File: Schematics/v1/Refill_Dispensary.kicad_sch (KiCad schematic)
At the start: 67 parts, among them J1 USB_B_Micro, J10 Switch 2, J11 Switch 3, J12 Switch 1, J13 SWD, J14 SWD, J15 Screen data, J16 Screen Backlight, J2 Pot 1, J3 Barrel_Jack_Switch, J4 USB_BOOT, J5 Load Cell Power, J6 Load Cell Data, J7 Inductor 1, J8 Inductor 2, J9 Pot 2, Q1 TIP120, Q2 TIP120, SW4 SW_SPDT, U1 RP2040, U2 NCP1117-3.3_SOT223, U3 Flash Memory, U5 AD622, Y1 Crystal

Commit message: cleanup
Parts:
- removed J15: Screen data, Connector_JST:JST_XH_B4B-XH-AM_1x04_P2.50mm_Vertical, symbol Connector_Generic:Conn_01x04
- removed J16: Screen Backlight, Connector_JST:JST_XH_B4B-XH-AM_1x04_P2.50mm_Vertical, symbol Connector_Generic:Conn_01x04
- added U4: NHD-C0220BIZ, Display:NHD-C0220BiZ, symbol Display_Character:NHD-C0220BIZ
- C1, C10, C13, C15, C16, C4, C7, C9: footprint Capacitor_SMD:C_0603_1608Metric_Pad1.08x0.95mm_HandSolder -> Capacitor_SMD:C_0402_1005Metric
- C11: value 1u -> 100n; footprint Capacitor_SMD:C_0603_1608Metric_Pad1.08x0.95mm_HandSolder -> Capacitor_SMD:C_0402_1005Metric
- C12: value 100n -> 1u; footprint Capacitor_SMD:C_0603_1608Metric_Pad1.08x0.95mm_HandSolder -> Capacitor_SMD:C_0201_0603Metric
- C14, C8: footprint Capacitor_SMD:C_0603_1608Metric_Pad1.08x0.95mm_HandSolder -> Capacitor_SMD:C_0201_0603Metric
- R1, R10, R11, R13, R14, R16, R2, R3, R4, R5, R6, R7, R8: footprint Resistor_SMD:R_0603_1608Metric_Pad0.98x0.95mm_HandSolder -> Resistor_SMD:R_0201_0603Metric
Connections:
- net +1V1: now also C1.2, C7.2; no longer C1.1, C7.1
- net +3.3V: now also C10.2, C11.2, C13.2, C15.2, C16.2, C9.2, R13.1, U4.5 (VDD), U4.9 (A); no longer C10.1, C11.1, C13.1, C15.1, C16.1, C9.1, R13.2
- net GND: now also C1.1, C10.1, C11.1, C13.1, C15.1, C16.1, C7.1, C9.1, U4.10 (K), U4.4 (VSS); no longer C1.2, C10.2, C11.2, C13.2, C15.2, C16.2, C7.2, C9.2
- net S_SCL: now also R13.2, U4.2 (SCL); no longer R13.1
- net S_SDA: now also U4.3 (SDA)
- net at C14.2: now also U4.8 (C1-)
- net at C14.1: now also U4.7 (C1+)
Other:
- moved on the sheet: C14, R10

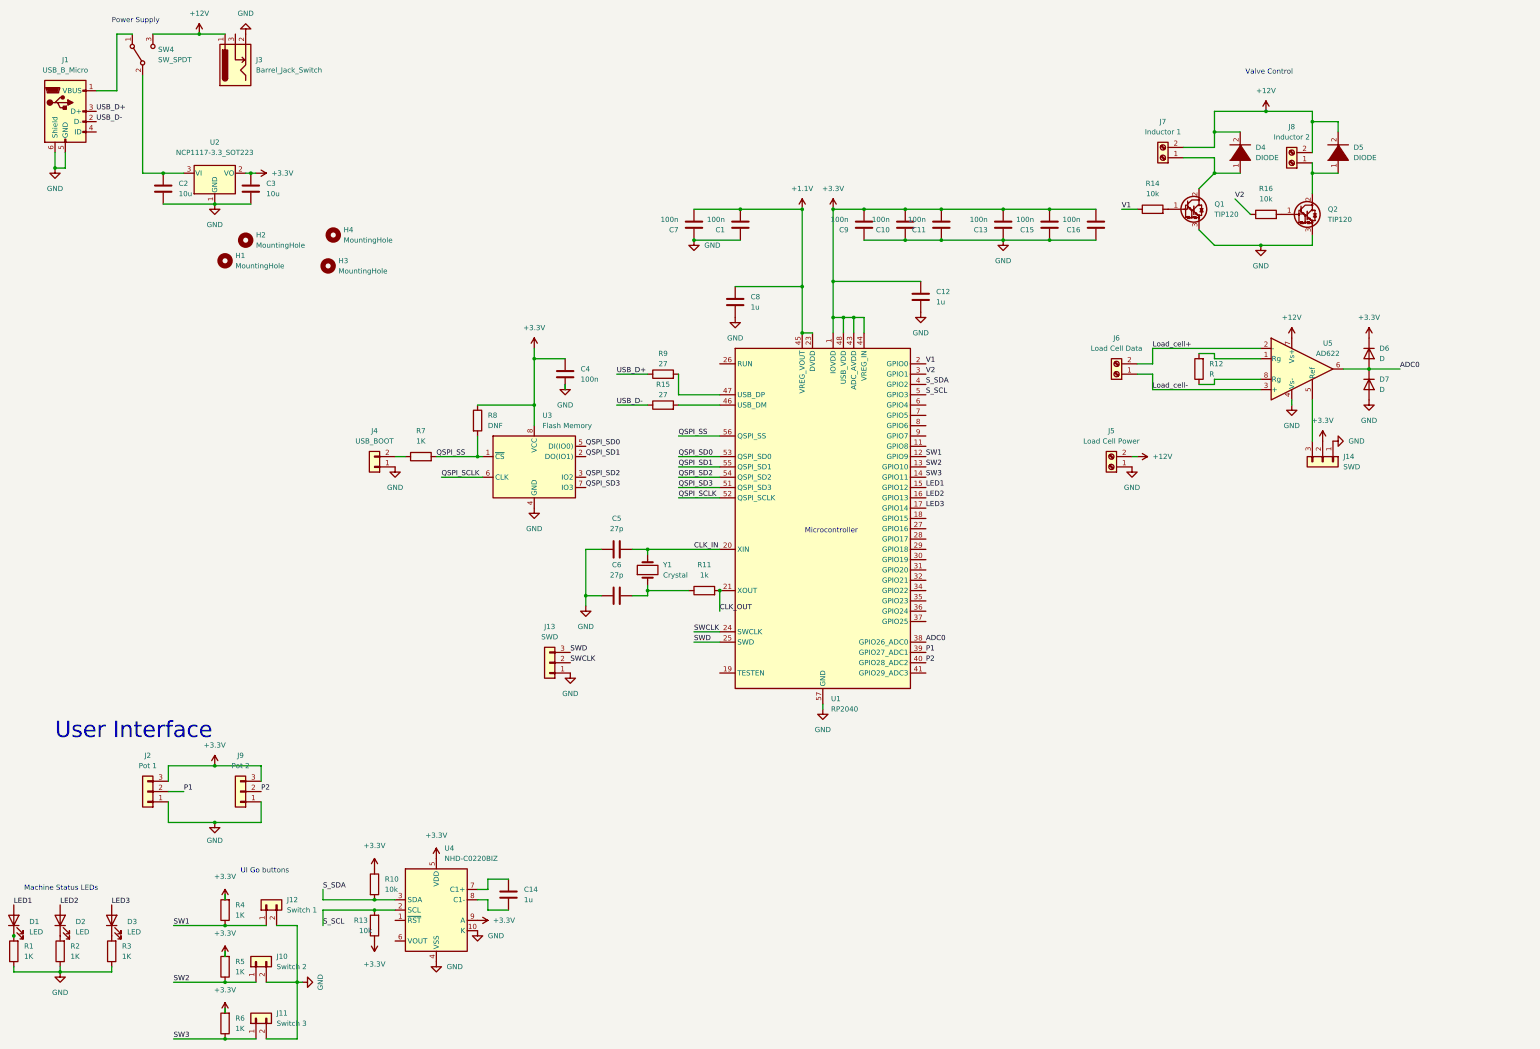
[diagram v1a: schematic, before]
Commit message: 1608:all routes connected
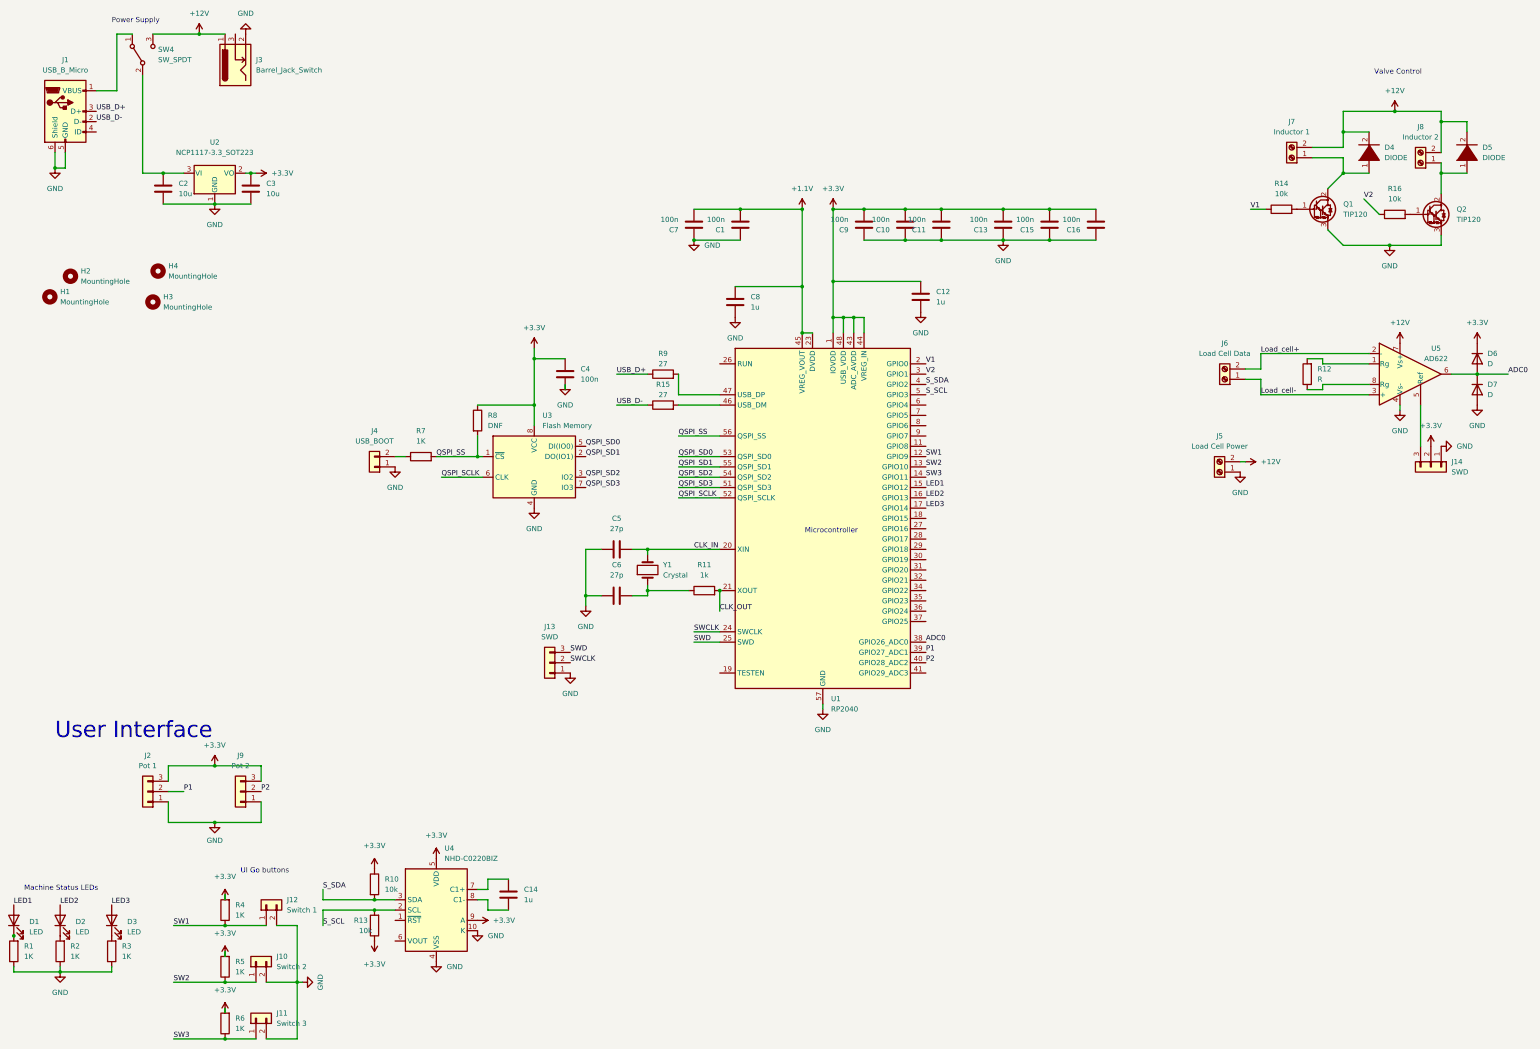
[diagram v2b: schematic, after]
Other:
- moved on the sheet: D4, D5, D6, D7, H1, H2, H3, H4, J14, J5, J6, J7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
